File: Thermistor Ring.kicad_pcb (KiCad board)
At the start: 2 copper layers, 48.3 x 48.3 mm, 18 parts, among them J1 Conn_01x04_Socket, U1 TPS7A2018PDBVR, U2 MCP9808T-E/MC, U3 MCP9808T-E/MC, U4 MCP9808T-E/MC, U5 MCP9808T-E/MC, U6 MCP9808T-E/MC, U7 MCP9808T-E/MC

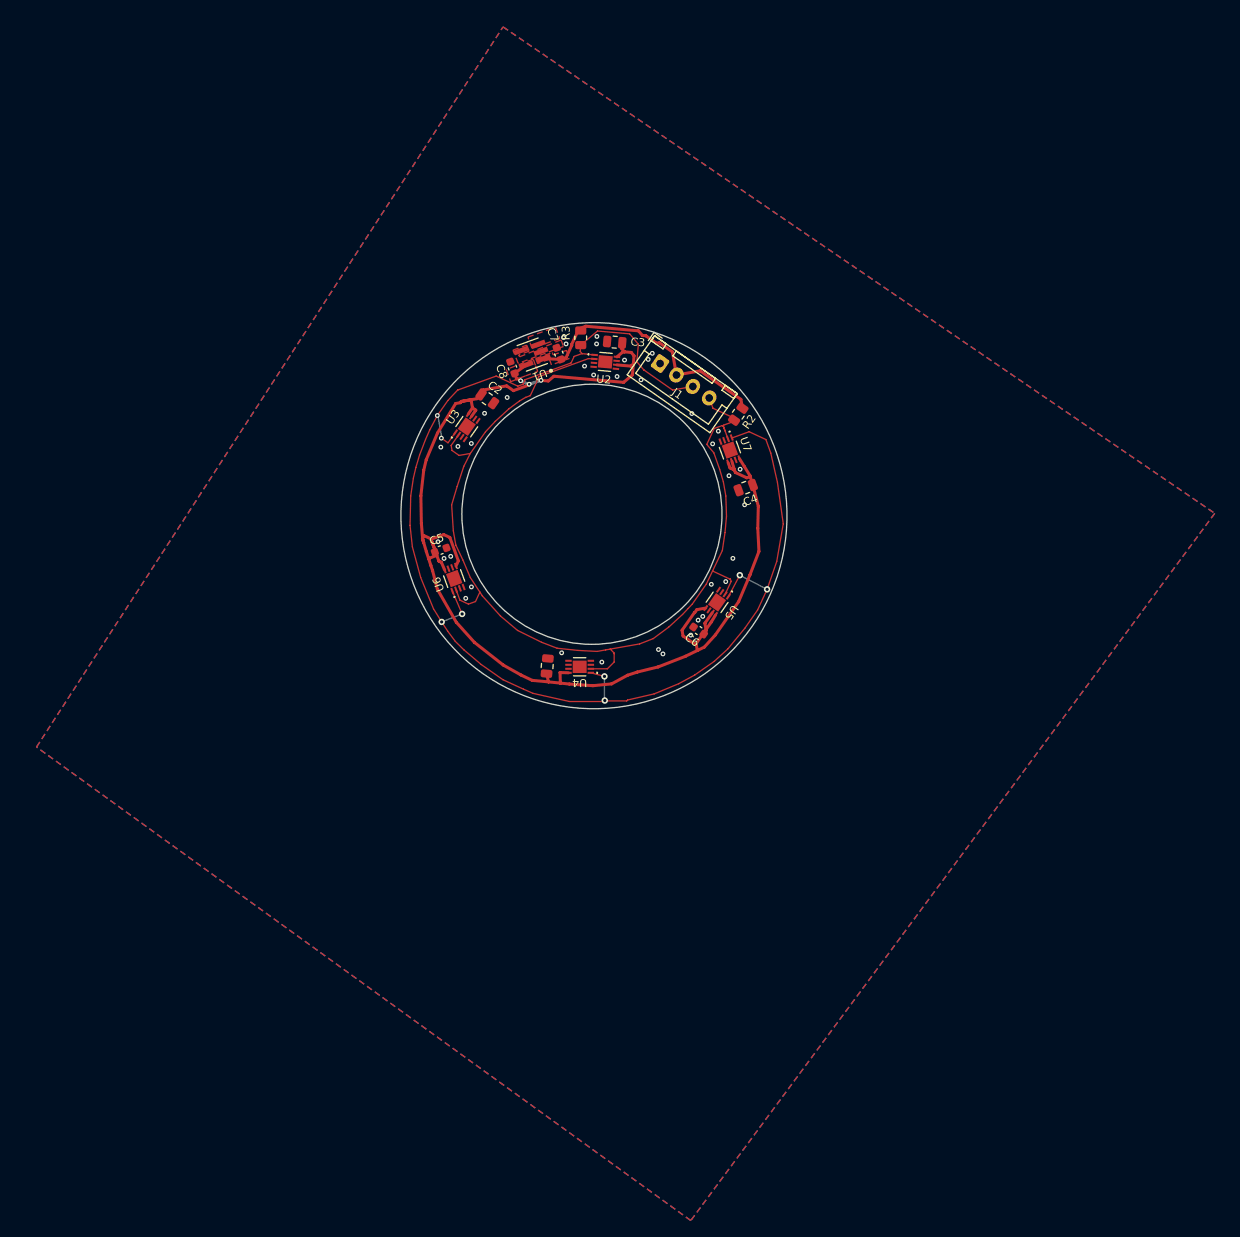
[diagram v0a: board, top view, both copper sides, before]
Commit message: Pass DRC and fix fills
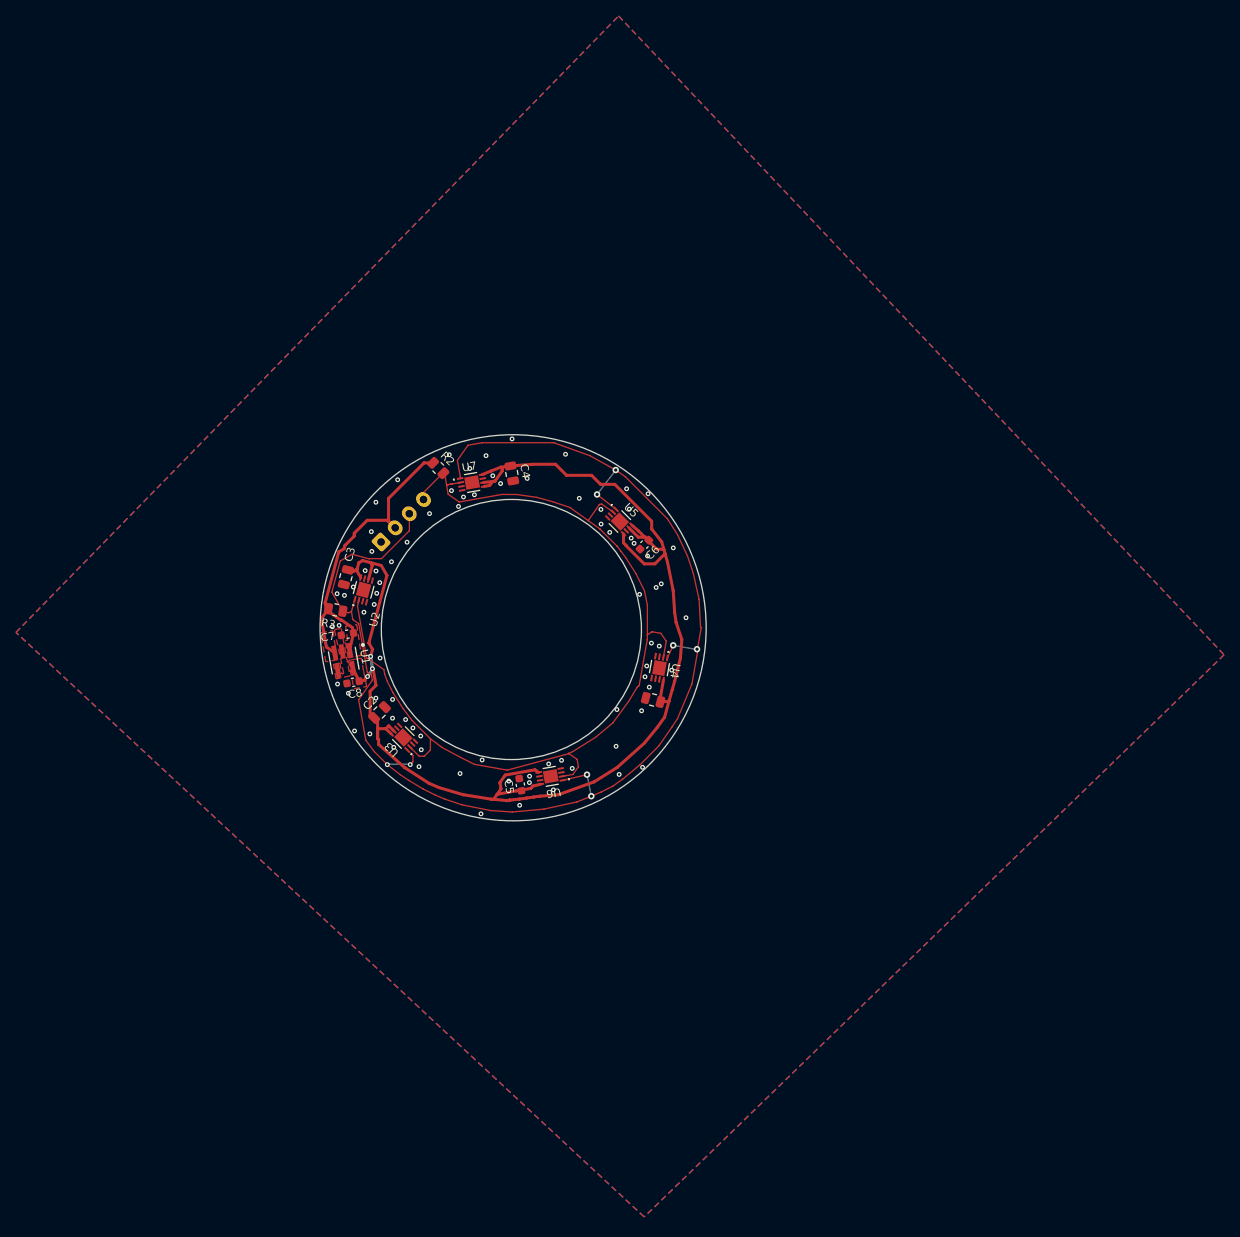
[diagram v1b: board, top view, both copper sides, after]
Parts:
- J1: moved to B.Cu
- moved R3 45.8 mm to (50.6, 62.0), turned to -10 degrees
- moved U1 44.9 mm to (51.7, 68.4), turned to -80 degrees
- moved C3 44.6 mm to (51.9, 57.9), turned to -105 degrees
- moved C8 44.1 mm to (52.8, 71.1), turned to -170 degrees
- moved C7 43.9 mm to (52.1, 65.1), turned to -170 degrees
- moved U2 41.5 mm to (54.1, 59.5), turned to 75 degrees
- moved C2 41.5 mm to (56.1, 74.9), turned to 45 degrees
- moved J1 41.4 mm to (56.3, 53.5), turned to 45 degrees
- moved U3 39.7 mm to (59.1, 78.0), turned to 135 degrees
- moved R2 38.1 mm to (63.5, 44.3), turned to -45 degrees
- moved U7 32.5 mm to (67.7, 46.1), turned to 10 degrees
- moved C5 31.0 mm to (73.7, 83.9), turned to 100 degrees
- moved C4 29.3 mm to (72.7, 45.0), turned to -80 degrees
- moved U6 27.5 mm to (77.5, 82.8), turned to -170 degrees
- moved U5 15.8 mm to (86.2, 51.0), turned to -45 degrees
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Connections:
- U1 pad 3: /ENABLE -> /Power 3.3-5V
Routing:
- net /Power 3.3-5V: track 32.8 -> 41.6 mm
- net /VDD: track 169.3 -> 170.7 mm
- net GND: track 0.00 -> 0.33 mm, vias 37 -> 81
- removed copper zone on F.Cu, net /ENABLE
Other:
- outline, holes or cut-outs redrawn

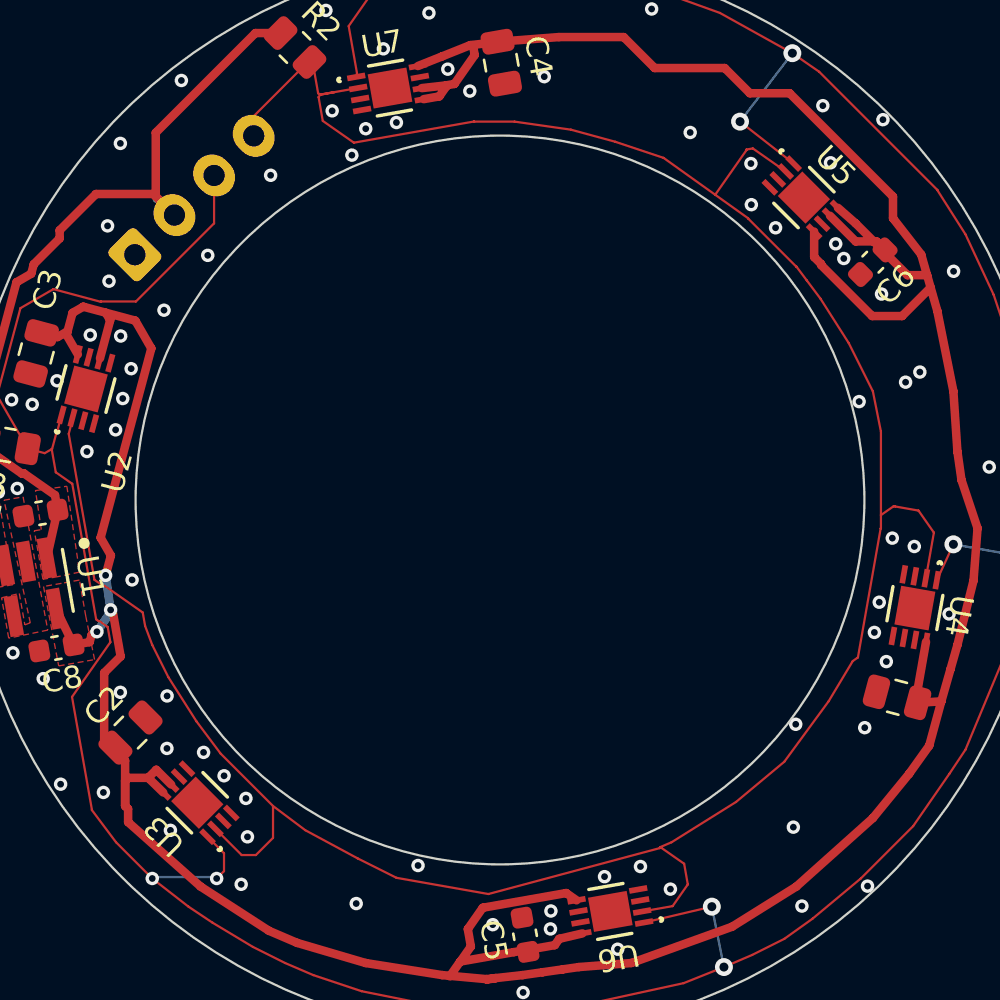
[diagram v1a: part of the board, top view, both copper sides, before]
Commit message: Addedtabs for potting
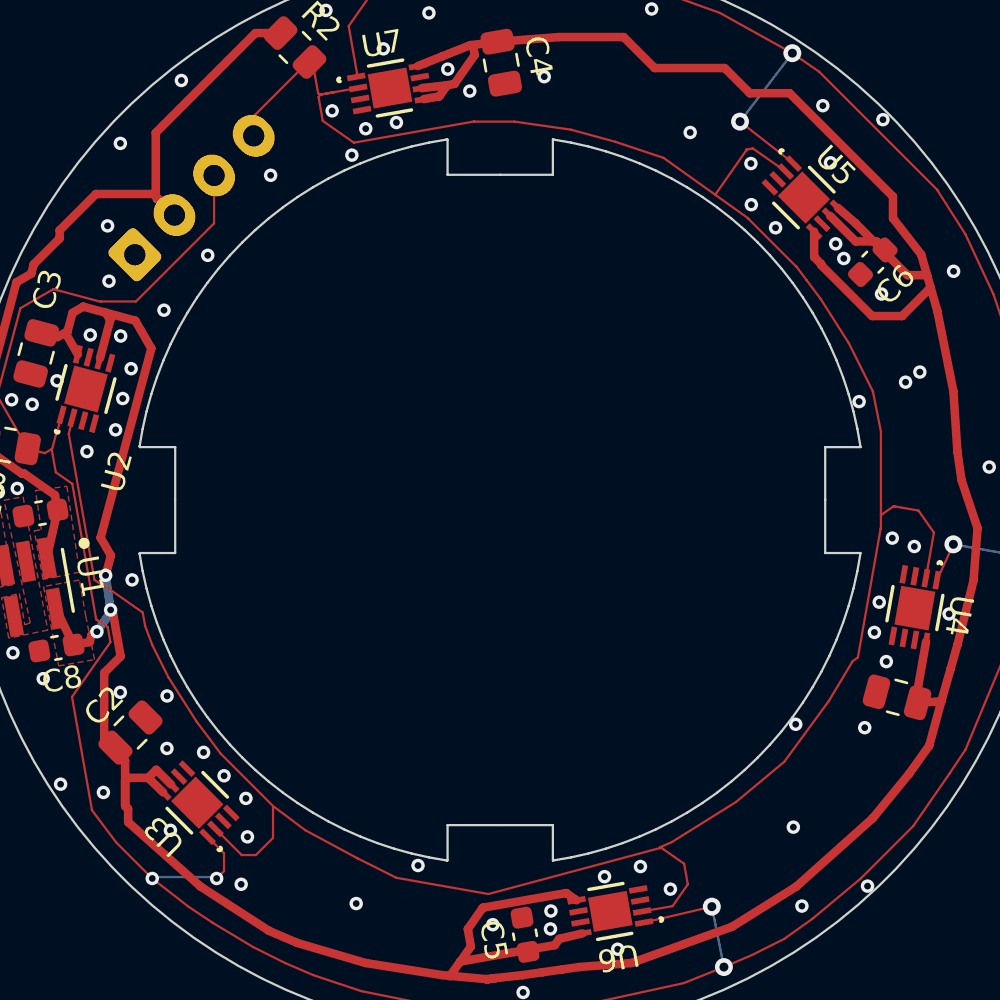
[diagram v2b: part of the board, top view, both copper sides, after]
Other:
- outline, holes or cut-outs redrawn

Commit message: Cleanup
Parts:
- moved R3 26.5 mm to (62.0, 38.1), turned to -55 degrees
- moved U1 25.9 mm to (58.2, 43.3), turned to -125 degrees
- moved C3 25.9 mm to (65.8, 36.1), turned to -150 degrees
- moved C8 25.4 mm to (57.1, 46.0), turned to 145 degrees
- moved C7 25.4 mm to (60.9, 41.3), turned to 145 degrees
- moved U2 24.0 mm to (66.2, 38.8), turned to 30 degrees
- moved C2 23.8 mm to (56.8, 51.0), turned to 0 degrees
- moved J1 23.5 mm to (72.0, 36.1), turned to 0 degrees
- moved U3 22.8 mm to (56.7, 55.3), turned to 90 degrees
- moved R2 22.3 mm to (83.6, 34.6), turned to -90 degrees
- moved U7 19.0 mm to (85.3, 38.9), turned to -35 degrees
- moved C5 17.7 mm to (62.9, 69.9), turned to 55 degrees
- moved C4 17.3 mm to (89.6, 41.6), turned to -125 degrees
- moved U6 15.7 mm to (66.3, 71.8), turned to 145 degrees
- moved U5 9.80 mm to (94.9, 55.4), turned to -90 degrees
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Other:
- outline, holes or cut-outs redrawn

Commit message: Add fiducials
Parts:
- added REF**: Fiducial_1.5mm_Mask3mm, Fiducial:Fiducial_1.5mm_Mask3mm, F.Cu at (57.3, 61.2)
- added REF**: Fiducial_1.5mm_Mask3mm, Fiducial:Fiducial_1.5mm_Mask3mm, F.Cu at (92.0, 45.6)
- added REF**: Fiducial_1.5mm_Mask3mm, Fiducial:Fiducial_1.5mm_Mask3mm, F.Cu at (77.8, 74.9)
- moved R2 0.19 mm to (83.7, 34.4)
- moved C3 0.19 mm to (65.9, 35.9)
- moved U2 0.19 mm to (66.3, 38.6)
- moved C8 0.19 mm to (57.2, 45.8)
- moved C6 0.19 mm to (95.1, 59.4)
- moved U5 0.19 mm to (95.0, 55.2)
- moved U4 0.19 mm to (85.6, 71.7)
- moved U3 0.19 mm to (56.8, 55.2)
- moved U6 0.19 mm to (66.4, 71.6)
- moved C4 0.19 mm to (89.7, 41.4)
- moved C5 0.19 mm to (62.9, 69.7)
- moved J1 0.19 mm to (72.1, 35.9)
- moved C1 0.19 mm to (82.2, 73.9)
- moved U1 0.19 mm to (58.3, 43.1)
- moved C7 0.19 mm to (61.0, 41.1)
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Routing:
- net GND: vias 81 -> 80

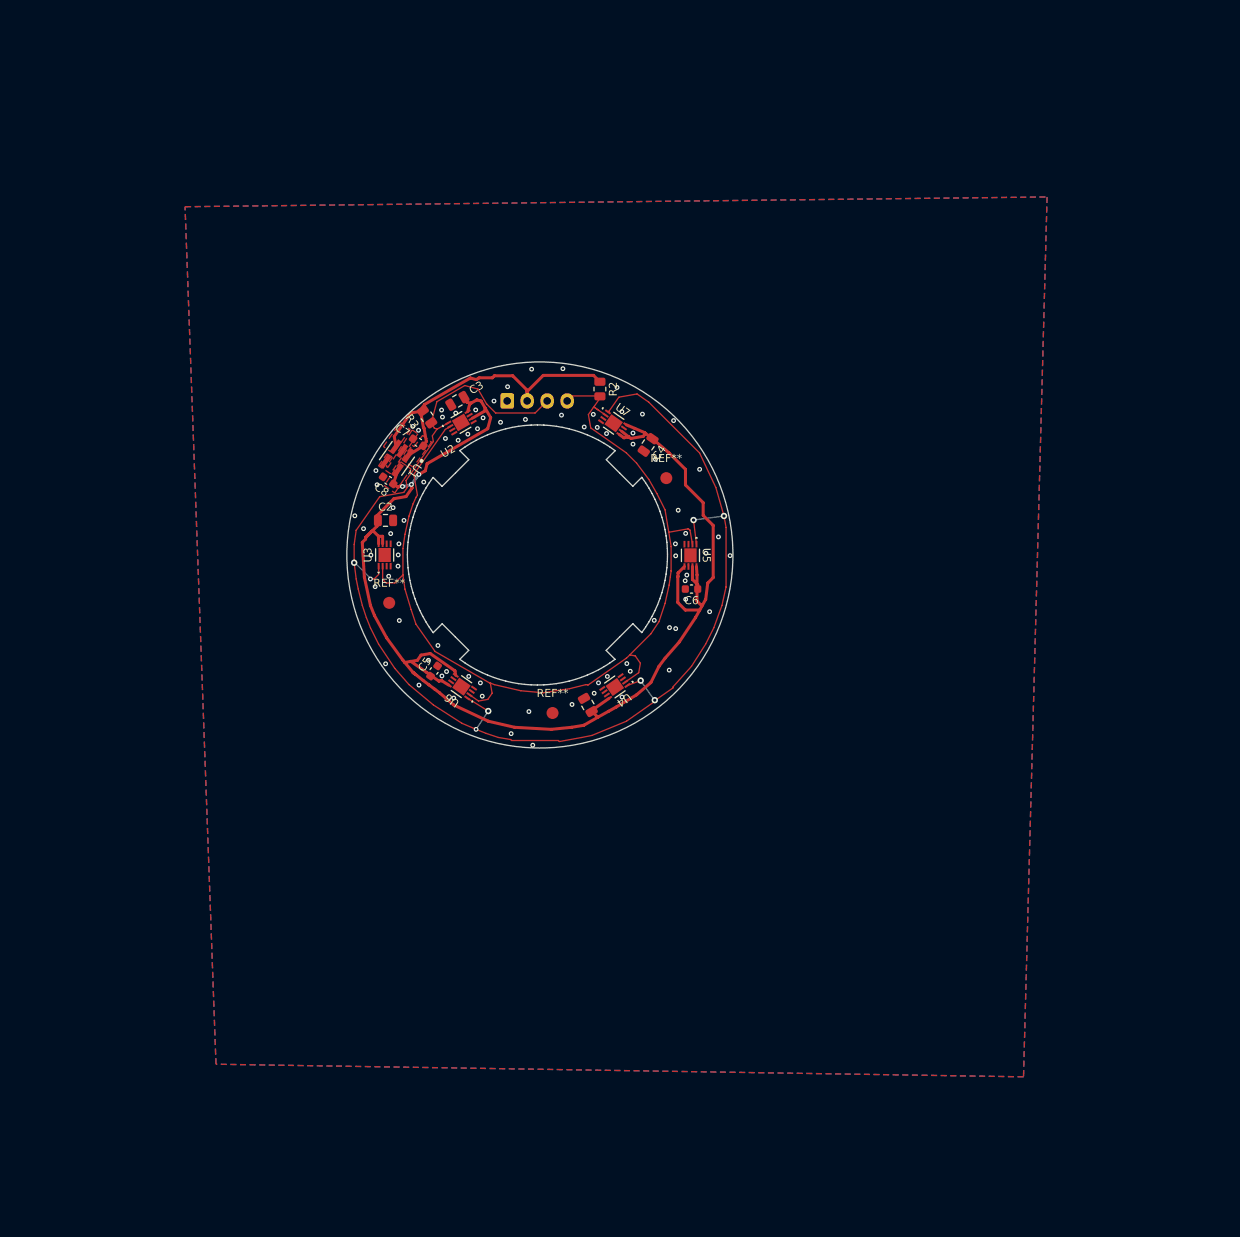
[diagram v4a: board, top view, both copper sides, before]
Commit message: Fixed fiducial silkscreen
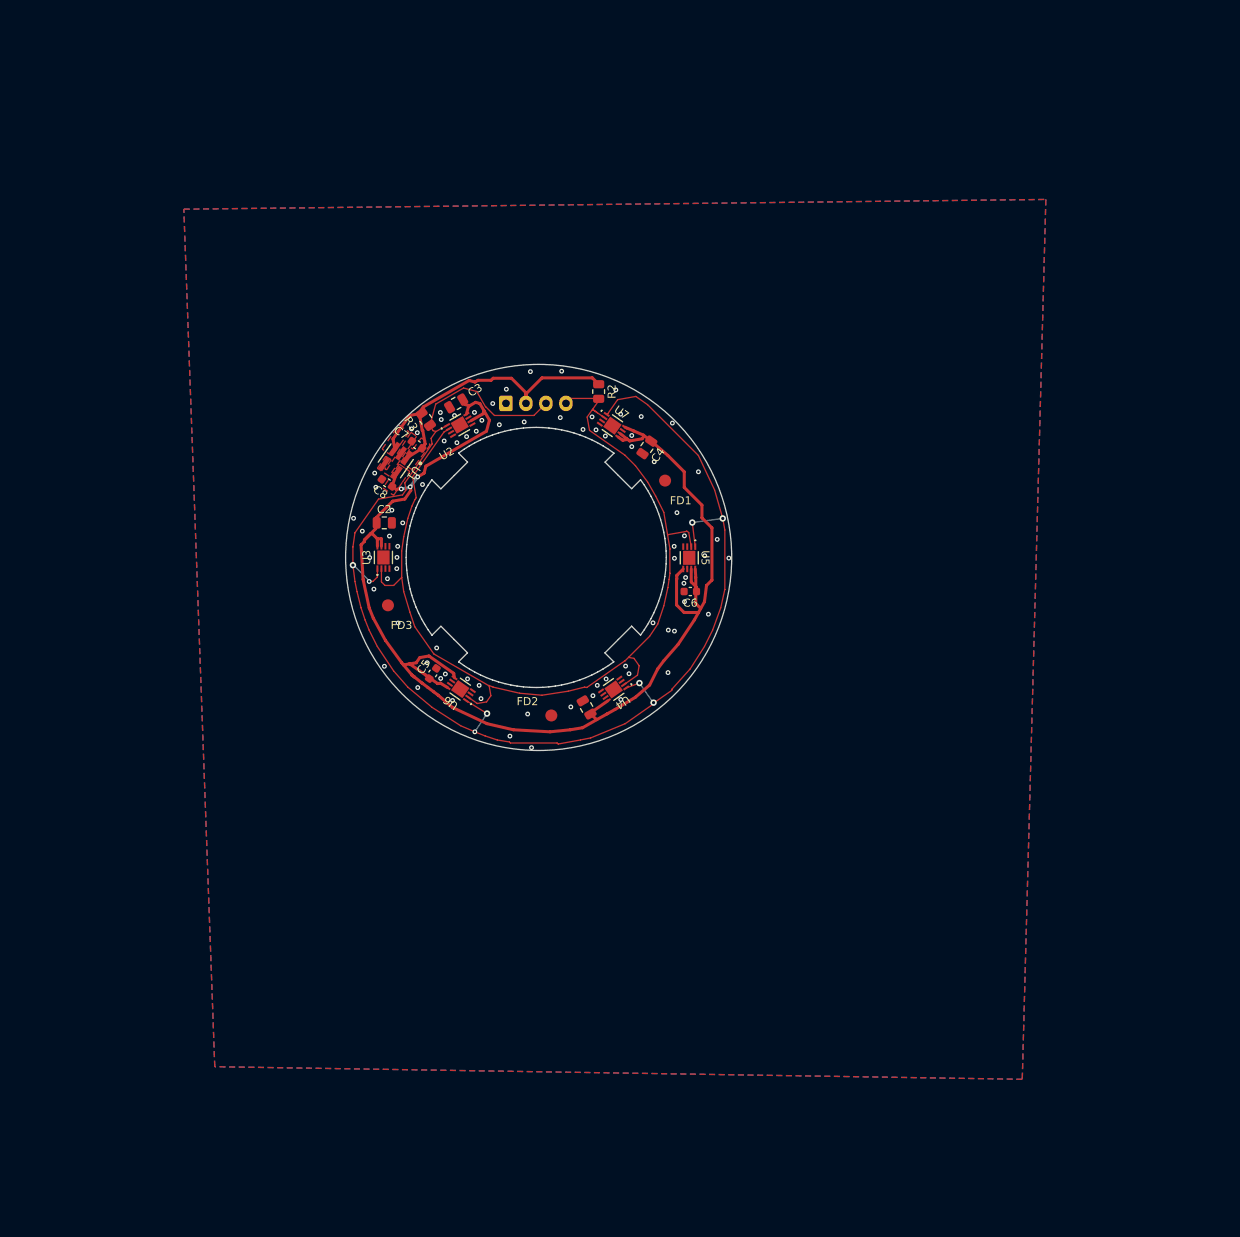
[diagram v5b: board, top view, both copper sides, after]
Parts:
- moved C3 0.35 mm to (65.7, 36.2)
- moved U6 0.35 mm to (66.2, 71.9)
- moved C5 0.35 mm to (62.8, 70.0)
- moved C8 0.35 mm to (57.1, 46.2)
- moved U5 0.35 mm to (94.8, 55.5)
- moved C2 0.35 mm to (56.7, 51.2)
- moved FD3 0.35 mm to (57.2, 61.5)
- moved FD1 0.35 mm to (91.8, 45.9)
- moved R3 0.35 mm to (61.9, 38.2)
- moved C1 0.35 mm to (82.0, 74.2)
- moved C6 0.35 mm to (95.0, 59.7)
- moved C7 0.35 mm to (60.8, 41.4)
- moved FD2 0.35 mm to (77.6, 75.2)
- moved R2 0.35 mm to (83.5, 34.7)
- moved U4 0.35 mm to (85.4, 72.0)
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- renumbered REF** to FD1, REF** to FD2, REF** to FD3
